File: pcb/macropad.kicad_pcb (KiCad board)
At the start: 2 copper layers, 62 x 81 mm, 34 parts, among them SW1 SW_Push, SW10 RotaryEncoder_Switch, SW2 SW_Push, SW3 SW_Push, SW4 SW_Push, SW5 SW_Push, SW6 SW_Push, SW7 SW_Push, SW8 SW_Push, SW9 SW_Push, U2 ER_OLEDM0.91_1x-I2C, U3 MOUDLE-SEEEDUINO-XIAO

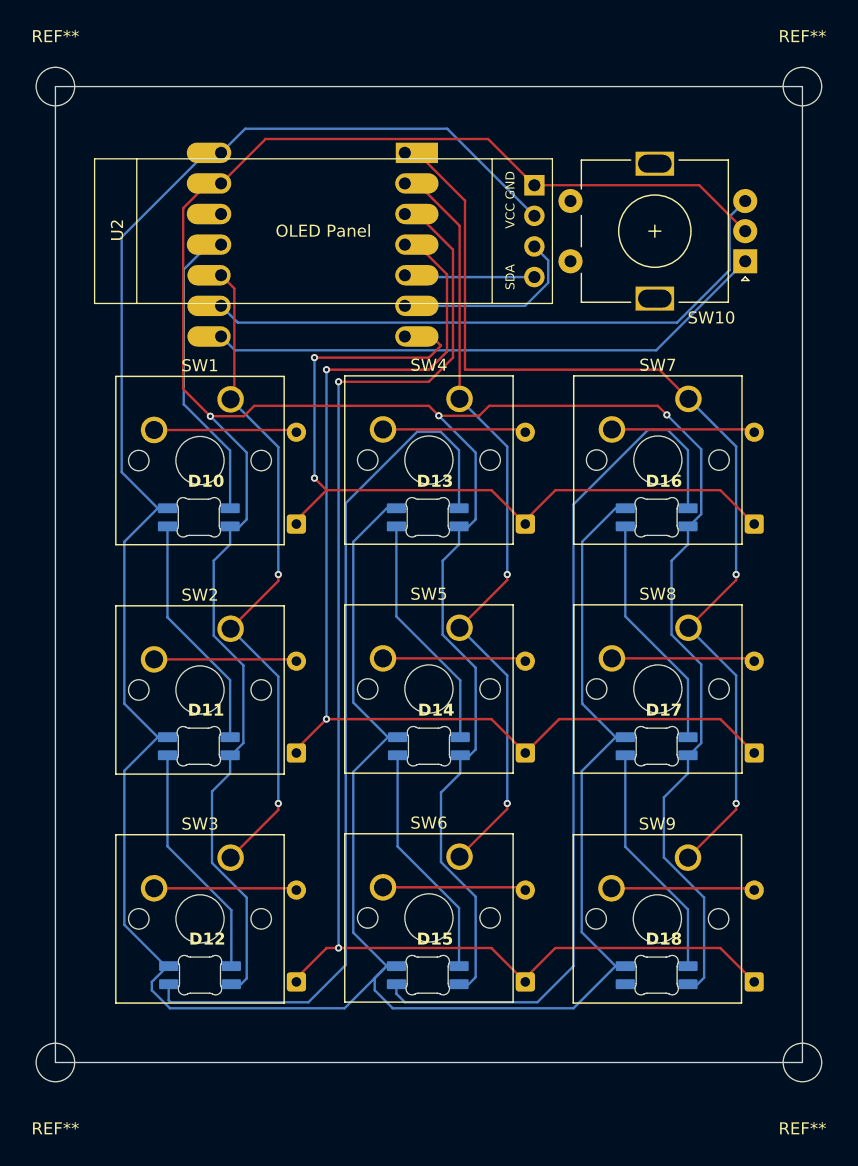
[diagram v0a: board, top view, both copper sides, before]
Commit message: created CAD assembly and assembled electronics and created bottom casing; also changed some electronics models
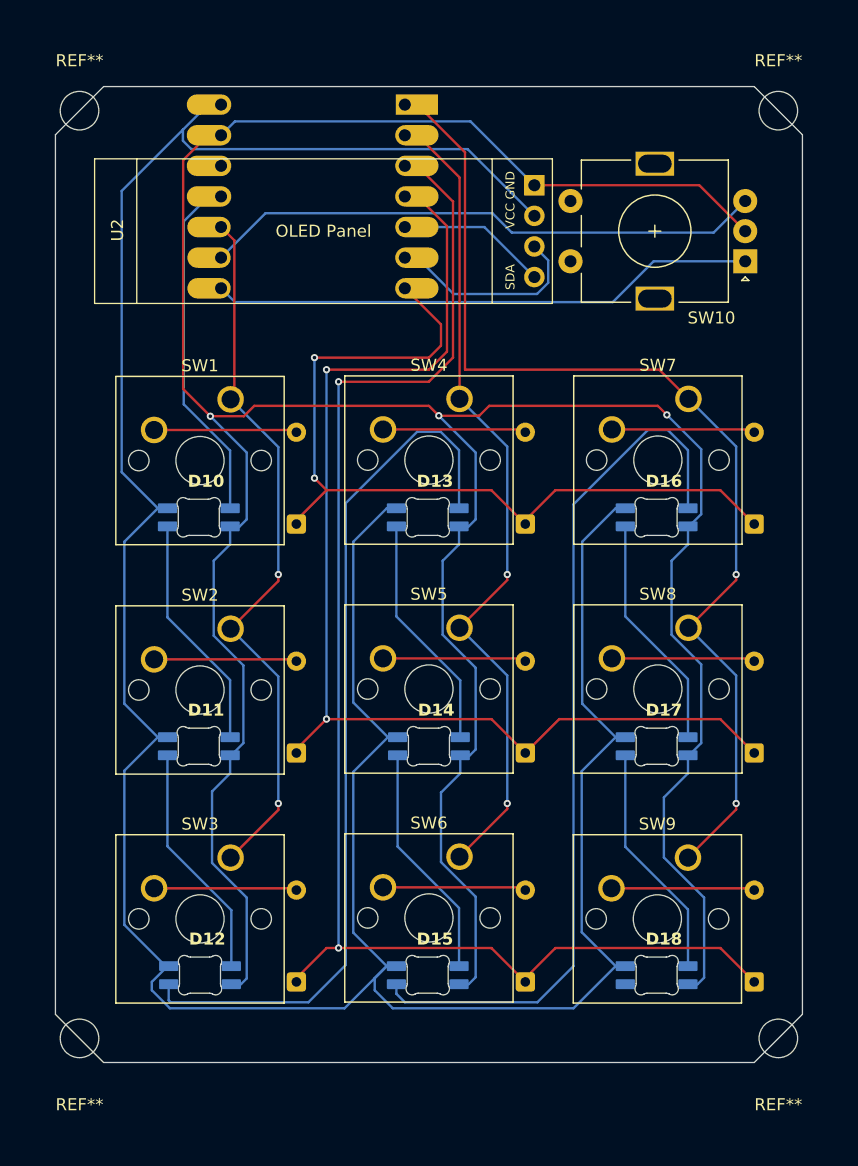
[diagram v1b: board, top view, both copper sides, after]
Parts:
- moved U3 4.00 mm to (68.9, 37.6)
- moved REF** 2.83 mm to (107.5, 107.5)
- moved REF** 2.83 mm to (49.5, 107.5)
- moved REF** 2.83 mm to (107.5, 30.5)
- moved REF** 2.83 mm to (49.5, 30.5)
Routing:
- net VCC: track 248.3 -> 255.0 mm
- net EC11B: track 50.9 -> 46.8 mm
- net row1: track 93.4 -> 97.4 mm
- net col0: track 55.5 -> 59.5 mm
- net col2: track 84.9 -> 88.9 mm
- net col1: track 64.9 -> 68.9 mm
- net WS28128B: track 25.4 -> 29.4 mm
- net GND: track 273.3 -> 276.9 mm
- net row2: track 115.6 -> 118.5 mm
- net row0: track 68.7 -> 71.4 mm
- net EC11A: track 47.0 -> 45.4 mm
- net SDA: track 10.8 -> 12.5 mm
- net SCL: track 16.2 -> 17.0 mm
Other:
- outline, holes or cut-outs redrawn

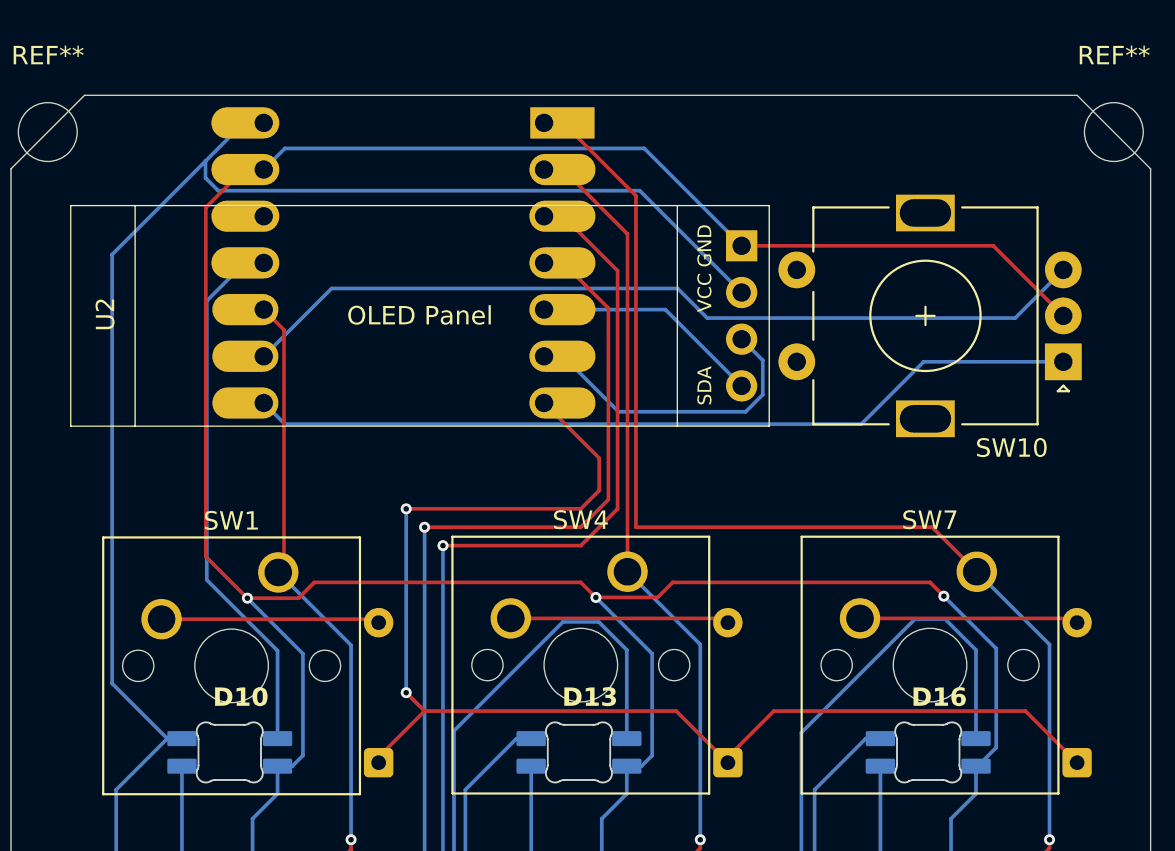
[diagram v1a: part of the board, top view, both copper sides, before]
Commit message: updated pcb and cad to align usb port
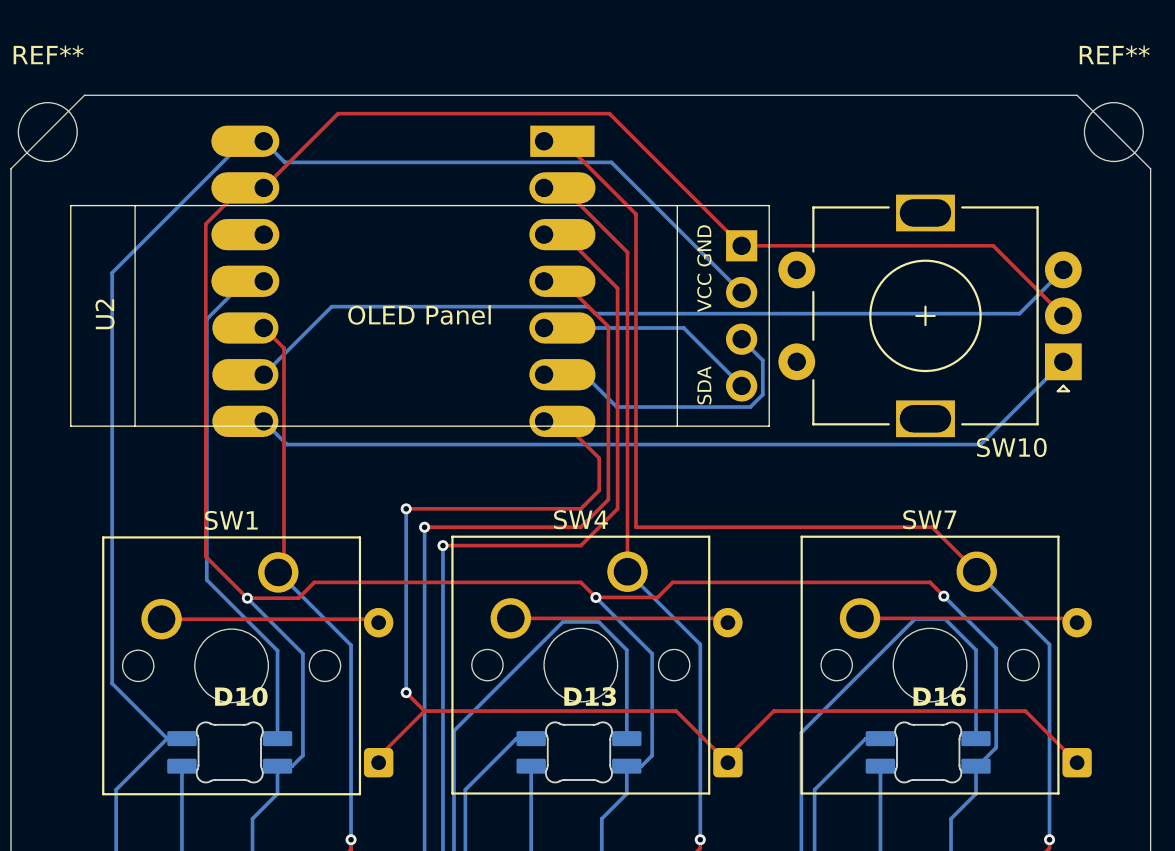
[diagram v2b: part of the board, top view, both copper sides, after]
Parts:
- moved U3 1.00 mm to (68.9, 38.6)
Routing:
- net VCC: track 255.0 -> 250.8 mm
- net GND: track 276.9 -> 277.9 mm
- net row1: track 97.4 -> 96.4 mm
- net col1: track 68.9 -> 67.9 mm
- net col0: track 59.5 -> 58.5 mm
- net WS28128B: track 29.4 -> 28.4 mm
- net col2: track 88.9 -> 87.9 mm
- net row2: track 118.5 -> 117.6 mm
- net SCL: track 17.0 -> 16.4 mm
- net EC11B: track 46.8 -> 46.2 mm
- net EC11A: track 45.4 -> 45.9 mm

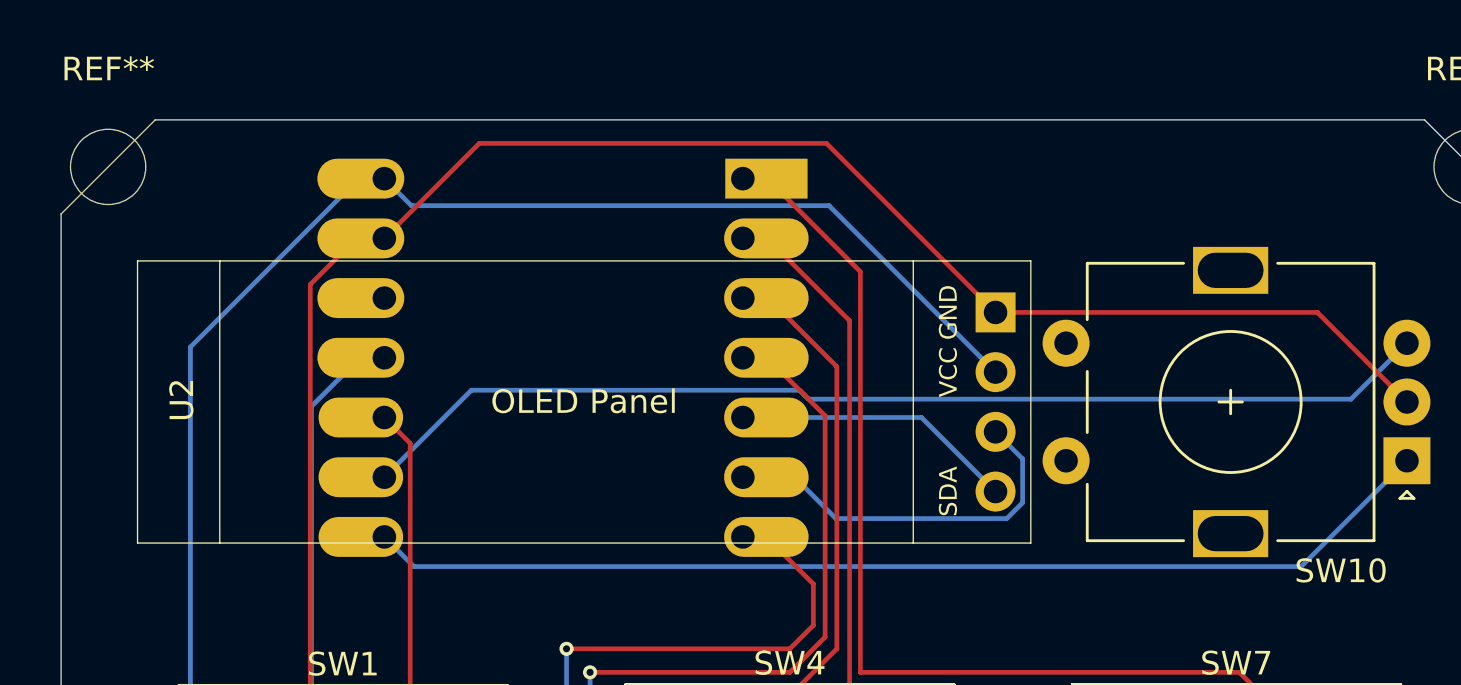
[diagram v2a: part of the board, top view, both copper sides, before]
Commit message: centered OLED
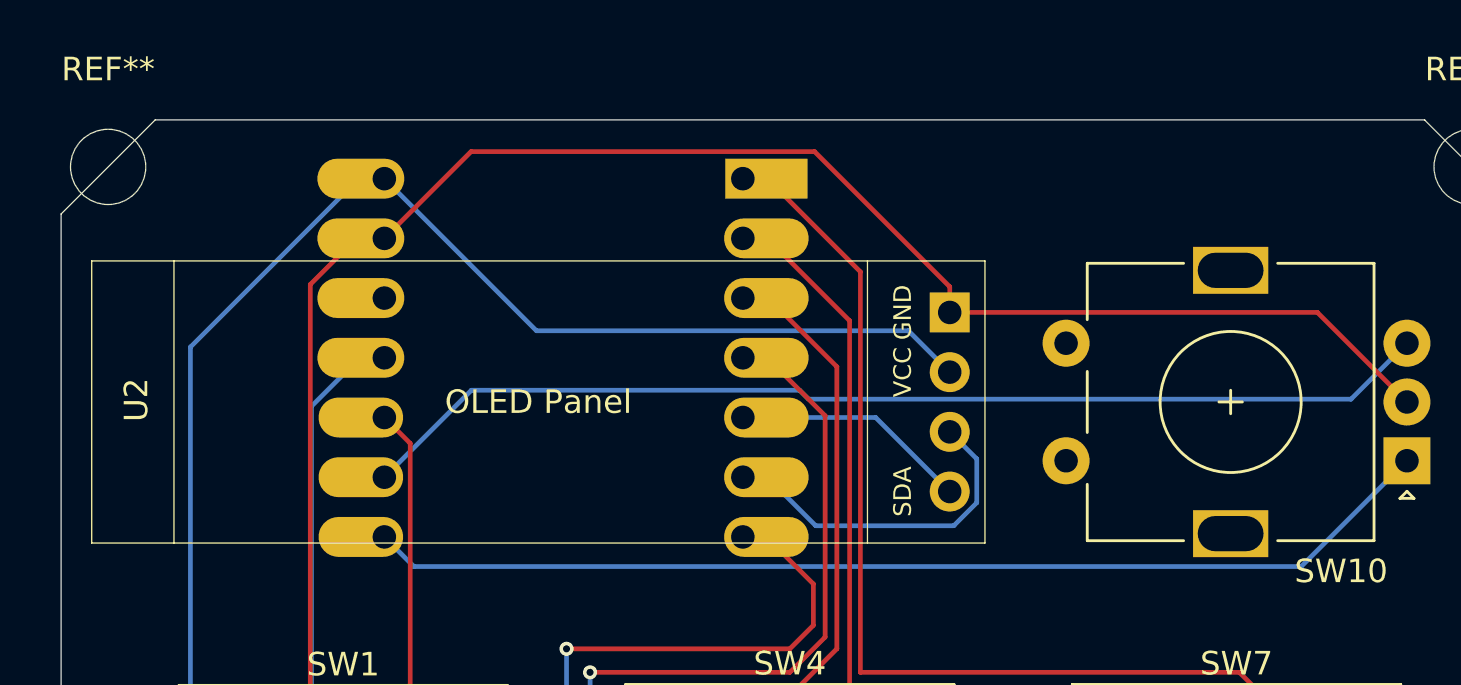
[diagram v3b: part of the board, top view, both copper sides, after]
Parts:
- moved U2 1.95 mm to (48.8, 34.5)
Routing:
- net VCC: track 250.8 -> 248.8 mm
- net SDA: track 12.1 -> 10.1 mm
- net SCL: track 16.4 -> 14.7 mm
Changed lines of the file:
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@@
 	(footprint "hackpad:SSD1306-0.91-OLED-4pin-128x32"
 		(layer "F.Cu")
-		(at 50.75 34.5)
+		(at 48.8 34.5)
 		(property "Reference" "U2"
 			(at 1.9 5.91 90)
@@
 	)
 	(segment
+		(start 85.3 35.6)
+		(end 79.55 29.85)
+		(width 0.2)
+		(layer "F.Cu")
+		(net "GND")
+	)
+	(segment
+		(start 100.94 36.69)
+		(end 85.3 36.69)
+		(width 0.2)
+		(layer "F.Cu")
+		(net "GND")
+	)
+	(segment
 		(start 58.1 53.6)
 		(end 58.1 35.5)
@@
 	)
 	(segment
-		(start 60.36 55.86)
-		(end 58.1 53.6)
+		(start 64.94 29.85)
+		(end 61.25 33.54)
 		(width 0.2)
 		(layer "F.Cu")
@@
 	)
 	(segment
-		(start 78.5 55)
-		(end 79.32 55.82)
+		(start 60.36 55.86)
+		(end 58.1 53.6)
 		(width 0.2)
 		(layer "F.Cu")
@@
 	)
 	(segment
-		(start 104.75 40.5)
-		(end 100.94 36.69)
+		(start 78.5 55)
+		(end 79.32 55.82)
 		(width 0.2)
 		(layer "F.Cu")
@@
 	)
 	(segment
-		(start 83.5 55)
-		(end 82.68 55.82)
+		(start 85.3 36.69)
+		(end 85.3 35.6)
 		(width 0.2)
 		(layer "F.Cu")
@@
 	)
 	(segment
-		(start 82.68 55.82)
-		(end 79.32 55.82)
+		(start 83.5 55)
+		(end 82.68 55.82)
 		(width 0.2)
 		(layer "F.Cu")
@@
 	)
 	(segment
-		(start 80.06 29.5)
-		(end 65.29 29.5)
+		(start 104.75 40.5)
+		(end 100.94 36.69)
 		(width 0.2)
 		(layer "F.Cu")
@@
 	)
 	(segment
-		(start 65.29 29.5)
-		(end 61.25 33.54)
+		(start 82.68 55.82)
+		(end 79.32 55.82)
 		(width 0.2)
 		(layer "F.Cu")
@@
 	)
 	(segment
-		(start 61.25 33.54)
-		(end 60.06 33.54)
+		(start 79.55 29.85)
+		(end 64.94 29.85)
 		(width 0.2)
 		(layer "F.Cu")
@@
 	)
 	(segment
-		(start 100.94 36.69)
-		(end 87.25 36.69)
+		(start 61.25 33.54)
+		(end 60.06 33.54)
 		(width 0.2)
 		(layer "F.Cu")
@@
 	)
 	(segment
-		(start 87.25 36.69)
-		(end 80.06 29.5)
-		(width 0.2)
-		(layer "F.Cu")
-		(net "GND")
-	)
-	(segment
 		(start 60.06 33.54)
 		(end 58.1 35.5)
@@
 	)
 	(segment
+		(start 83.54 37.47)
+		(end 67.72 37.47)
+		(width 0.2)
+		(layer "B.Cu")
+		(net "VCC")
+	)
+	(segment
 		(start 56 63.5)
 		(end 53 60.5)
@@
 	)
 	(segment
-		(start 80.17 32.15)
-		(end 62.4 32.15)
-		(width 0.2)
-		(layer "B.Cu")
-		(net "VCC")
-	)
-	(segment
 		(start 74 103.5)
 		(end 75.5 105)
@@
 	)
 	(segment
-		(start 62.4 32.15)
-		(end 61.25 31)
+		(start 85.3 39.23)
+		(end 83.54 37.47)
 		(width 0.2)
 		(layer "B.Cu")
@@
 	)
 	(segment
-		(start 87.25 39.23)
-		(end 80.17 32.15)
-		(width 0.2)
-		(layer "B.Cu")
-		(net "VCC")
-	)
-	(segment
 		(start 75 101.5)
 		(end 74 102.5)
@@
 	)
 	(segment
+		(start 67.72 37.47)
+		(end 61.25 31)
+		(width 0.2)
+		(layer "B.Cu")
+		(net "VCC")
+	)
+	(segment
 		(start 56 63.5)
 		(end 53.22 66.28)
@@
 	)
 	(segment
-		(start 80.46 45.46)
-		(end 78.7 43.7)
+		(start 86.45 44.786346)
+		(end 85.472692 45.763654)
 		(width 0.2)
 		(layer "B.Cu")
@@
 	)
 	(segment
-		(start 78.7 43.7)
-		(end 76.5 43.7)
+		(start 85.3 41.77)
+		(end 86.45 42.92)
 		(width 0.2)
 		(layer "B.Cu")
@@
 	)
 	(segment
-		(start 87.726346 45.46)
-		(end 80.46 45.46)
+		(start 79.6 45.763654)
+		(end 77.536346 43.7)
 		(width 0.2)
 		(layer "B.Cu")
@@
 	)
 	(segment
-		(start 88.4 44.786346)
-		(end 87.726346 45.46)
+		(start 85.472692 45.763654)
+		(end 79.6 45.763654)
 		(width 0.2)
 		(layer "B.Cu")
@@
 	)
 	(segment
-		(start 87.25 41.77)
-		(end 88.4 42.92)
+		(start 86.45 42.92)
+		(end 86.45 44.786346)
 		(width 0.2)
 		(layer "B.Cu")
@@
 	)
 	(segment
-		(start 88.4 42.92)
-		(end 88.4 44.786346)
+		(start 77.536346 43.7)
+		(end 76.5 43.7)
 		(width 0.2)
 		(layer "B.Cu")
@@
 	)
 	(segment
-		(start 84.1 41.16)
-		(end 76.5 41.16)
+		(start 85.3 44.31)
+		(end 82.15 41.16)
 		(width 0.2)
 		(layer "B.Cu")
@@
 	)
 	(segment
-		(start 87.25 44.31)
-		(end 84.1 41.16)
+		(start 82.15 41.16)
+		(end 76.5 41.16)
 		(width 0.2)
 		(layer "B.Cu")
